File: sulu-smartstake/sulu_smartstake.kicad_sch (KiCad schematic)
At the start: 25 parts, among them J1 Conn_01x08, J2 Conn_01x02, J3 Conn_02x12_Odd_Even, J4 73391-0060, J4 through_hole, M0 NP, M1 NP, M2 NP, M3 NP, M4 NP, M5 NP, M6 NP, M7 NP, U1 TPS62222DDCT, U2 TLV71311PDBV, U4 SN74LV4051ADR, U5 SN74LV4051ADR

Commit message: Modify schematics after review
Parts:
- removed J3: Conn_02x12_Odd_Even, Connector_PinHeader_2.54mm:PinHeader_2x12_P2.54mm_Vertical, symbol Connector_Generic:Conn_02x12_Odd_Even
- added J3, J4: Conn_02x08_Odd_Even, Connector_PinHeader_2.54mm:PinHeader_2x08_P2.54mm_Vertical, symbol Connector_Generic:Conn_02x08_Odd_Even
- added J6: Conn_01x03, Connector_PinHeader_2.54mm:PinHeader_1x03_P2.54mm_Vertical, symbol Connector_Generic:Conn_01x03
- added J7: Conn_01x02, Connector_PinHeader_2.54mm:PinHeader_1x02_P2.54mm_Vertical, symbol Connector_Generic:Conn_01x02
- M0, M1, M2, M3, M4, M5, M6, M7: footprint Capacitor_SMD:C_0603_1608Metric -> Capacitor_SMD:C_0805_2012Metric
- renumbered C4 to C2, C2 to C3, C3 to C4, J4 to J5
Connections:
- net +1.1V_REG: now also J7.1 (Pin_1)
- net +1.8V_REG: now also J6.1 (Pin_1); no longer U5.3 (X)
- net GND: now also J4.10 (Pin_10), J4.12 (Pin_12), J4.14 (Pin_14), J4.16 (Pin_16), J4.2 (Pin_2), J4.4 (Pin_4), J4.6 (Pin_6), J4.8 (Pin_8)
- net SENSOR_EXCITE0: now also J3.2 (Pin_2)
- net SENSOR_EXCITE1: now also J3.4 (Pin_4)
- net SENSOR_EXCITE2: now also J3.6 (Pin_6)
- net SENSOR_EXCITE3: now also J3.8 (Pin_8)
- net SENSOR_EXCITE4: now also J3.10 (Pin_10)
- net SENSOR_EXCITE5: now also J3.12 (Pin_12)
- net SENSOR_EXCITE6: now also J3.14 (Pin_14)
- net SENSOR_EXCITE7: now also J3.16 (Pin_16)
- net SENSOR_IN0: now also J3.1 (Pin_1), J4.1 (Pin_1)
- net SENSOR_IN1: now also J3.3 (Pin_3), J4.3 (Pin_3)
- net SENSOR_IN2: now also J3.5 (Pin_5), J4.5 (Pin_5)
- net SENSOR_IN3: now also J3.7 (Pin_7), J4.7 (Pin_7)
- net SENSOR_IN4: now also J3.9 (Pin_9), J4.9 (Pin_9)
- net SENSOR_IN5: now also J3.11 (Pin_11), J4.11 (Pin_11)
- net SENSOR_IN6: now also J3.13 (Pin_13), J4.13 (Pin_13)
- net SENSOR_IN7: now also J3.15 (Pin_15), J4.15 (Pin_15)
- new net +1.1V_IN: J7.2 (Pin_2)
- new net EXCITE_IN: J6.2 (Pin_2), U5.3 (X)
- new net SCUM_GPIO_8: J6.3 (Pin_3)
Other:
- note added: "Arc the connections to GND at SMA De-cram the layout (make layout twice as big, move EXT_BAT and regulators to one side, move muxes left) Add 4 screw holes for mounting"
- note removed: "Move 2 GNDs to the top Change common to a 3 pins - 1.8 V, common, GPIO for header flexibility Add in row of SENSOR_INx pins Add a 2x1 header connection for 1.1V REG Arc the connections to GND at SMA De-cram the layout (make layout twice as big, move EXT_BAT and regulators to one side, move muxes left) Add 4 screw holes for mounting Change M components to 0805 Important note: if the 1.1 V regulato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"
- moved on the sheet: C1, C2, C3, C4, J1, J2, L2, M0, M1, M2, M3, M4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

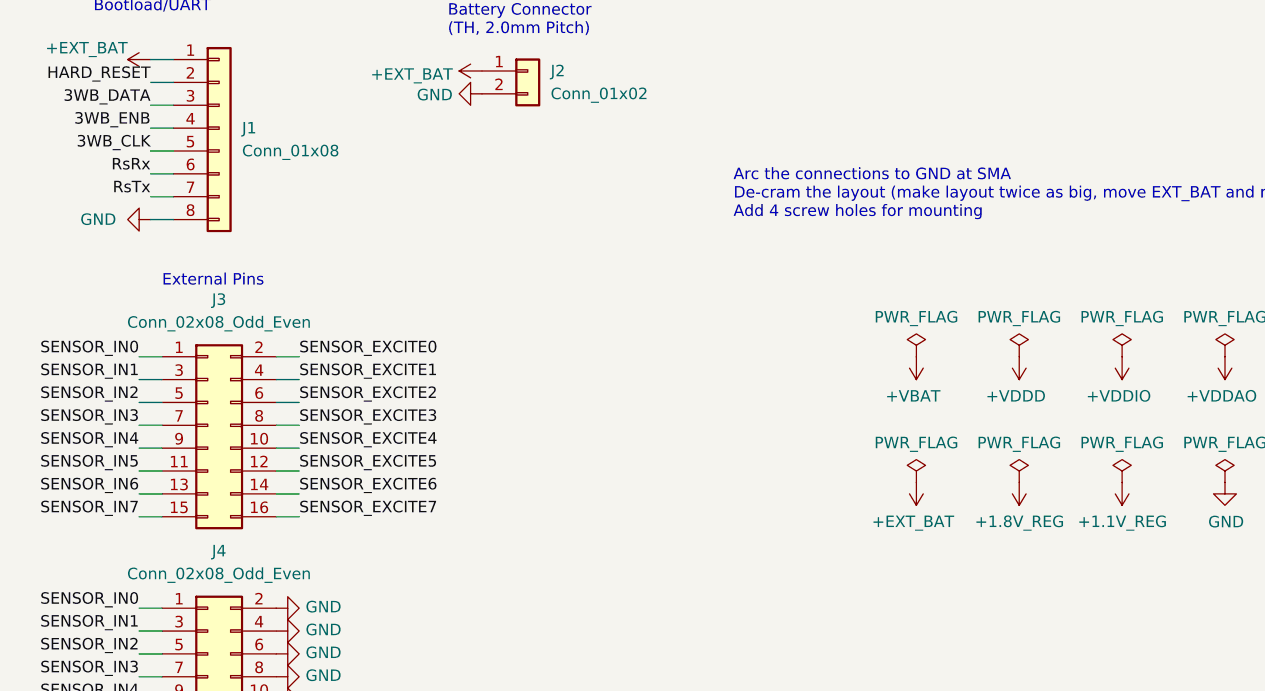
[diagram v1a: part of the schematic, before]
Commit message: Finalize layout footprint
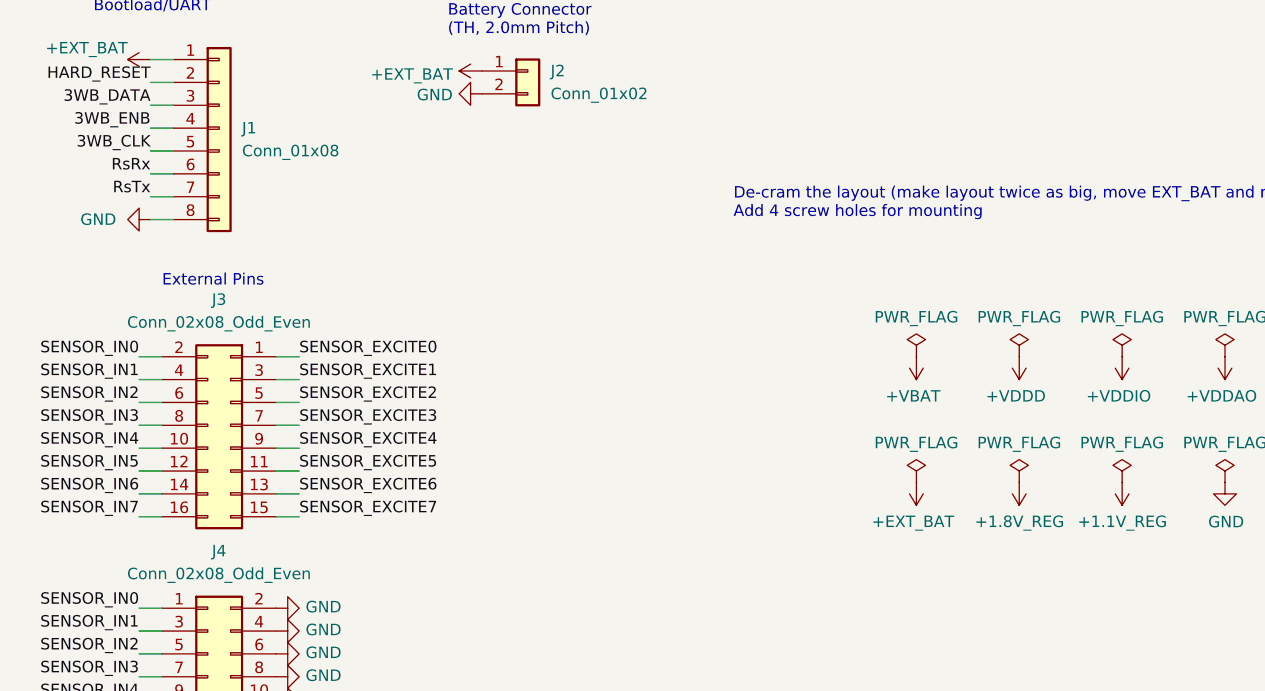
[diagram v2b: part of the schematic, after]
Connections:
- net SENSOR_EXCITE0: now also J3.1 (Pin_1); no longer J3.2 (Pin_2)
- net SENSOR_EXCITE1: now also J3.3 (Pin_3); no longer J3.4 (Pin_4)
- net SENSOR_EXCITE2: now also J3.5 (Pin_5); no longer J3.6 (Pin_6)
- net SENSOR_EXCITE3: now also J3.7 (Pin_7); no longer J3.8 (Pin_8)
- net SENSOR_EXCITE4: now also J3.9 (Pin_9); no longer J3.10 (Pin_10)
- net SENSOR_EXCITE5: now also J3.11 (Pin_11); no longer J3.12 (Pin_12)
- net SENSOR_EXCITE6: now also J3.13 (Pin_13); no longer J3.14 (Pin_14)
- net SENSOR_EXCITE7: now also J3.15 (Pin_15); no longer J3.16 (Pin_16)
- net SENSOR_IN0: now also J3.2 (Pin_2); no longer J3.1 (Pin_1)
- net SENSOR_IN1: now also J3.4 (Pin_4); no longer J3.3 (Pin_3)
- net SENSOR_IN2: now also J3.6 (Pin_6); no longer J3.5 (Pin_5)
- net SENSOR_IN3: now also J3.8 (Pin_8); no longer J3.7 (Pin_7)
- net SENSOR_IN4: now also J3.10 (Pin_10); no longer J3.9 (Pin_9)
- net SENSOR_IN5: now also J3.12 (Pin_12); no longer J3.11 (Pin_11)
- net SENSOR_IN6: now also J3.14 (Pin_14); no longer J3.13 (Pin_13)
- net SENSOR_IN7: now also J3.16 (Pin_16); no longer J3.15 (Pin_15)
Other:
- note added: "De-cram the layout (make layout twice as big, move EXT_BAT and regulators to one side, move muxes left) Add 4 screw holes for mounting"
- note removed: "Arc the connections to GND at SMA De-cram the layout (make layout twice as big, move EXT_BAT and regulators to one side, move muxes left) Add 4 screw holes for mounting"
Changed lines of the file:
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@@
     (effects (font (size 1.27 1.27)) (justify left bottom))
   )
-  (text "Arc the connections to GND at SMA\nDe-cram the layout (make layout twice as big, move EXT_BAT and regulators to one side, move muxes left)\nAdd 4 screw holes for mounting"
+  (text "De-cram the layout (make layout twice as big, move EXT_BAT and regulators to one side, move muxes left)\nAdd 4 screw holes for mounting"
     (at 186.69 121.92 0)
     (effects (font (size 1.27 1.27)) (justify left bottom))
@@
     )
   )
-  (symbol (lib_id "Connector_Generic:Conn_02x08_Odd_Even") (at 128.27 144.78 0) (unit 1)
-    (in_bom yes) (on_board yes) (dnp no) (fields_autoplaced)
+  (symbol (lib_id "Connector_Generic:Conn_02x08_Odd_Even") (at 130.81 144.78 0) (mirror y) (unit 1)
+    (in_bom yes) (on_board yes) (dnp no)
     (property "Reference" "J3" (at 129.54 130.81 0)
       (effects (font (size 1.27 1.27)))
@@
       (effects (font (size 1.27 1.27)))
     )
-    (property "Footprint" "Connector_PinHeader_2.54mm:PinHeader_2x08_P2.54mm_Vertical" (at 128.27 144.78 0)
-      (effects (font (size 1.27 1.27)) hide)
-    )
-    (property "Datasheet" "~" (at 128.27 144.78 0)
-      (effects (font (size 1.27 1.27)) hide)
-    )
+    (property "Footprint" "Connector_PinHeader_2.54mm:PinHeader_2x08_P2.54mm_Vertical" (at 130.81 144.78 0)
+      (effects (font (size 1.27 1.27)) hide)
+    )
+    (property "Datasheet" "~" (at 130.81 144.78 0)
+      (effects (font (size 1.27 1.27)) hide)
+    )

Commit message: Finished layout after review
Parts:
- added J4: through_hole, SCUM:through_hole, symbol draft1library:through_hole
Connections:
- net SCUM_GPIO_8 is gone; now on net SCUM_GPIO8: J6.3 (Pin_3)
- net SENSOR_EXT_IN: now also J4.1 (pin)
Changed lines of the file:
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@@
     (effects (font (size 1.27 1.27)) (justify right bottom))
   )
-  (label "SCUM_GPIO_8" (at 142.24 63.5 180) (fields_autoplaced)
+  (label "SCUM_GPIO8" (at 142.24 63.5 180) (fields_autoplaced)
     (effects (font (size 1.27 1.27)) (justify right bottom))
   )
@@
   )
   (label "3WB_DATA" (at 121.92 109.22 180) (fields_autoplaced)
+    (effects (font (size 1.27 1.27)) (justify right bottom))
+  )
+  (label "SENSOR_EXT_IN" (at 279.4 68.58 270) (fields_autoplaced)
     (effects (font (size 1.27 1.27)) (justify right bottom))
   )
@@
         )
       )
+    )
+  )
+  (symbol (lib_id "draft1library:through_hole") (at 279.4 68.58 90) (unit 1)
+    (in_bom yes) (on_board yes) (dnp no)
+    (property "Reference" "J4" (at 274.32 68.58 0)
+      (effects (font (size 1.27 1.27)) hide)
+    )
+    (property "Value" "through_hole" (at 276.86 68.58 0)
+      (effects (font (size 1.27 1.27)) hide)
+    )
+    (property "Footprint" "SCUM:through_hole" (at 279.4 68.58 0)
+      (effects (font (size 1.27 1.27)) hide)
+    )
+    (property "Datasheet" "" (at 279.4 68.58 0)
+      (effects (font (size 1.27 1.27)) hide)
+    )
+    (pin "1")
+    (instances
+      (project "sulu_smartstake"
+        (path "/def6aede-50f9-4865-b84d-079828465adb/1f92f92f-1391-4fc3-892c-7c652348c5b5"
+          (reference "J4") (unit 1)
+        )
+        (path "/def6aede-50f9-4865-b84d-079828465adb"
+          (reference "J9") (unit 1)
+        )
+      )

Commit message: Final touches
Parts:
- removed J4 (x2): through_hole, SCUM:through_hole, symbol draft1library:through_hole
- added J5: Conn_02x03_Odd_Even, Connector_PinHeader_2.54mm:PinHeader_2x03_P2.54mm_Vertical, symbol Connector_Generic:Conn_02x03_Odd_Even
- renumbered J5 to J8
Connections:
- net +1.1V_IN: now also J5.3 (Pin_3)
- net +1.8V_REG: now also J5.1 (Pin_1)
- net GND: now also J5.2 (Pin_2), J5.4 (Pin_4)
- net SENSOR_EXT_IN: now also J5.6 (Pin_6)
- net SENSOR_LDO_OUTPUT: now also J5.5 (Pin_5)
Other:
- note added: "Debug Pins"
- note removed: "De-cram the layout (make layout twice as big, move EXT_BAT and regulators to one side, move muxes left) Add 4 screw holes for mounting"
- moved on the sheet: C1, C2, C3, C4, J2, J3, J4, J7, L2, U1, U2
